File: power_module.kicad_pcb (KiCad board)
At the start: 2 copper layers, 6 parts, among them J1 USB_B, J2 CONN_01X02

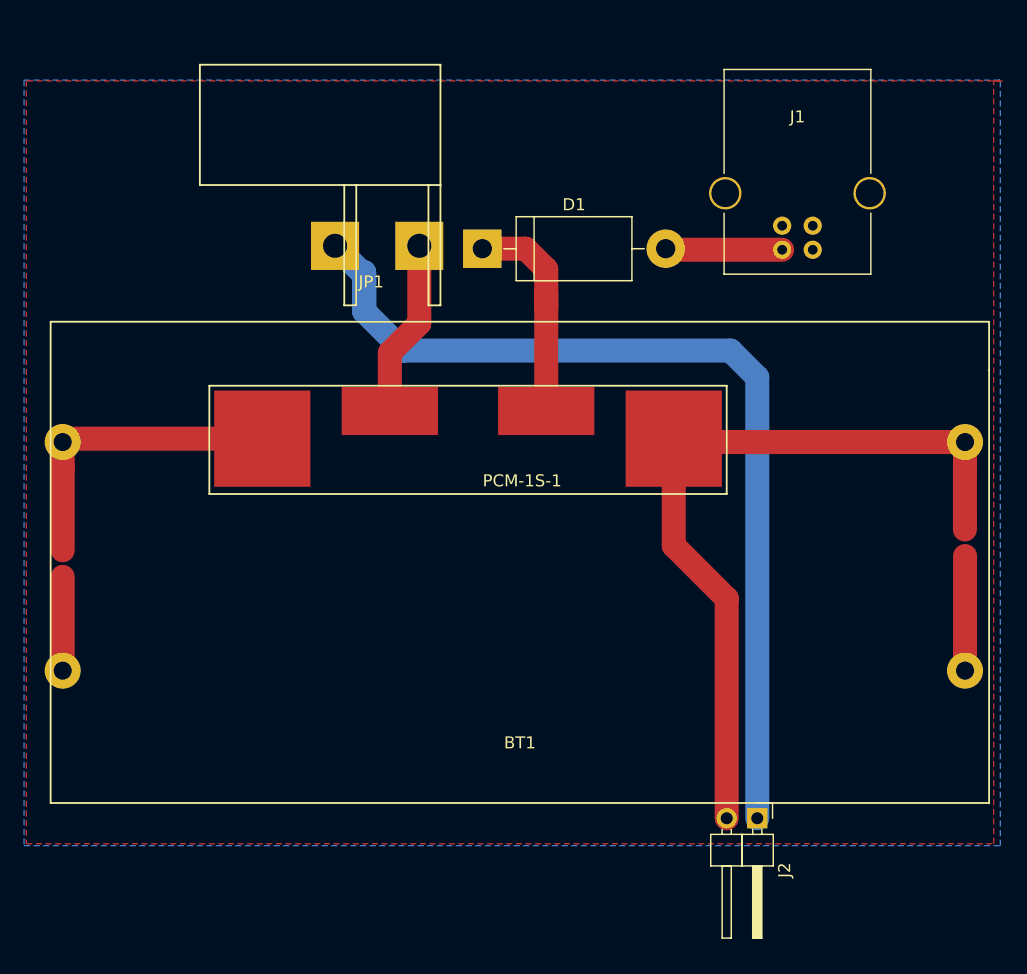
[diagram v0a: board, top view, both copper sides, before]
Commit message: add attiny 24-ssu
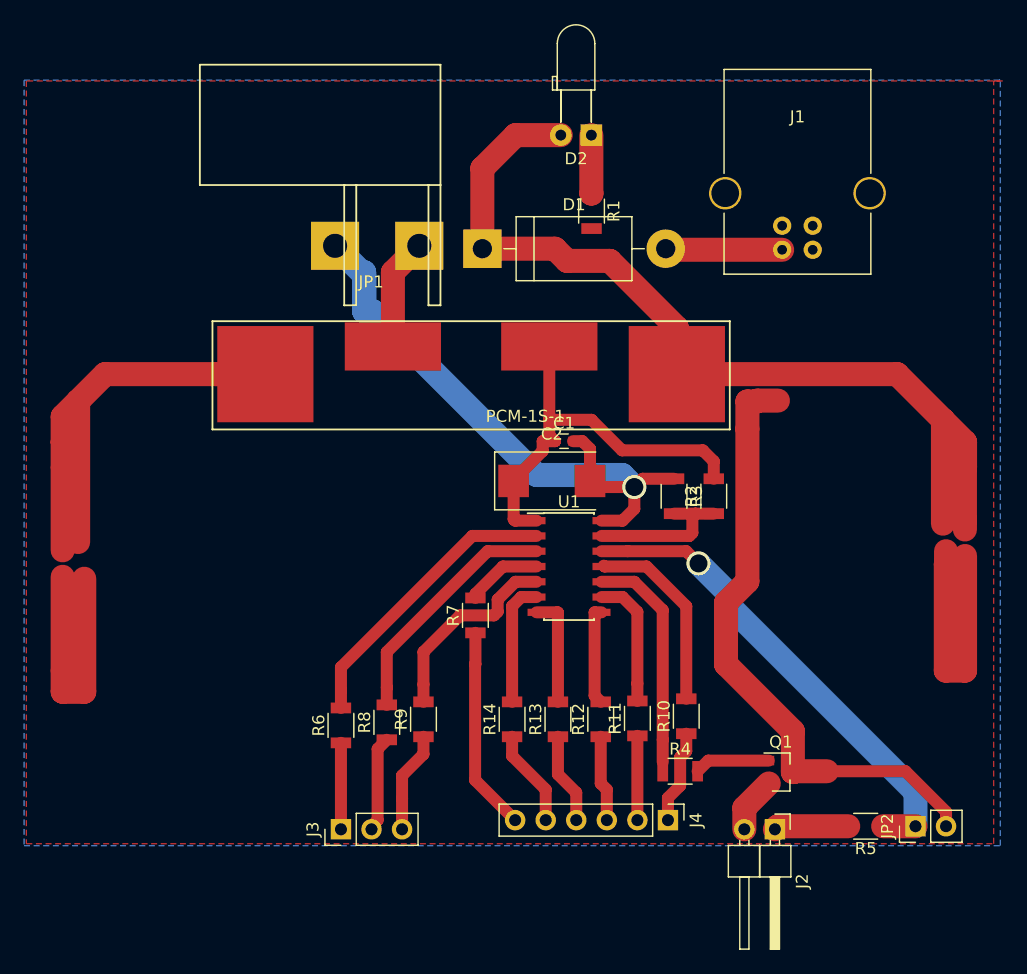
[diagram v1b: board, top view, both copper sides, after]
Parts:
- removed BT1: Battery, BH-18650-PC4
- added C1: 0.1uF, Capacitors_SMD:C_0603, F.Cu at (113.0, 67.3)
- added C2: 4.7uF, Capacitors_Tantalum_SMD:CP_Tantalum_Case-D_EIA-7343-31_Reflow, F.Cu at (112.0, 70.6)
- added D2: LED, LEDs:LED_D3.0mm_Horizontal_O3.81mm_Z6.0mm, F.Cu at (115.3, 41.9)
- added J3: CONN_01X03, Pin_Headers:Pin_Header_Straight_1x03_Pitch2.54mm, F.Cu at (94.5, 99.6)
- added J4: CONN_01X06, Pin_Headers:Pin_Header_Straight_1x06_Pitch2.54mm, F.Cu at (121.7, 98.8)
- added JP2: Jumper, Pin_Headers:Pin_Header_Straight_1x02_Pitch2.54mm, F.Cu at (142.2, 99.3)
- added Q1: Q_NMOS_GSD, TO_SOT_Packages_SMD:SOT-23, F.Cu at (131.0, 94.8)
- added R1: R, Resistors_SMD:R_1206, F.Cu at (115.3, 48.2)
- added R10: R, Resistors_SMD:R_1206, F.Cu at (123.2, 90.2)
- added R11: R, Resistors_SMD:R_1206, F.Cu at (119.1, 90.3)
- added R12: R, Resistors_SMD:R_1206, F.Cu at (116.1, 90.4)
- added R13: R, Resistors_SMD:R_1206, F.Cu at (112.5, 90.4)
- added R14: R, Resistors_SMD:R_1206, F.Cu at (108.7, 90.4)
- added R2: R, Resistors_SMD:R_1206, F.Cu at (125.5, 71.9)
- added R3: R, Resistors_SMD:R_1206, F.Cu at (122.2, 71.9)
- added R4: R, Resistors_SMD:R_1206, F.Cu at (122.7, 94.7)
- added R5: R, Resistors_SMD:R_1206, F.Cu at (138.1, 99.3)
- added R6: R, Resistors_SMD:R_1206, F.Cu at (94.5, 90.9)
- added R7: R, Resistors_SMD:R_1206, F.Cu at (105.7, 81.8)
- added R8: R, Resistors_SMD:R_1206, F.Cu at (98.3, 90.7)
- added R9: R, Resistors_SMD:R_1206, F.Cu at (101.3, 90.4)
- added U1: ATTINY24A-SSU, Housings_SOIC:SOIC-14_3.9x8.7mm_Pitch1.27mm, F.Cu at (113.4, 77.7)
- PCM-1S-1: footprint XZD-YH10A-1 -> XZD-YH10A-1:XZD-YH10A-1
- moved PCM-1S-1 5.37 mm to (105.8, 61.3)
- moved J2 1.73 mm to (130.6, 99.6)
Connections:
- J2 pad 2: Net-(BT1-Pad1) -> Net-(J2-Pad2)
- PCM-1S-1 pad 1: Net-(BT1-Pad1) -> +4V
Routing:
- net +4V: track 0.00 -> 87.1 mm
- net Net-(JP2-Pad1): track 0.00 -> 40.5 mm, vias 0 -> 1
- net (no net): track 17.3 -> 41.8 mm
- net Net-(R6-Pad2): track 0.00 -> 24.2 mm
- net Net-(R8-Pad2): track 0.00 -> 20.3 mm
- net Net-(C1-Pad2): track 81.3 -> 61.2 mm, vias 0 -> 1
- net Net-(R4-Pad1): track 0.00 -> 18.7 mm
- net Net-(J4-Pad6): track 0.00 -> 17.0 mm
- net Net-(R9-Pad2): track 0.00 -> 16.5 mm
- net Net-(R10-Pad2): track 0.00 -> 15.9 mm
- net Net-(BT1-Pad2): track 25.7 -> 41.5 mm
- net Net-(R2-Pad1): track 0.00 -> 12.7 mm
- net Net-(R11-Pad2): track 0.00 -> 10.9 mm
- net Net-(R14-Pad2): track 0.00 -> 10.3 mm
- net Net-(R13-Pad2): track 0.00 -> 9.20 mm
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
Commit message: Correct pcb
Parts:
- added BT1: Battery, BH-18650-PC4:BH-18650-PC4, F.Cu at (236.5, 65.5)
- added R15: 47K, Resistors_SMD:R_1206, F.Cu at (253.2, 80.5)
- C1: footprint Capacitors_SMD:C_0603 -> Capacitors_SMD:C_0805
- J2: value CONN_01X02 -> VOUT
- R1, R3: value R -> 330
- R2: value R -> 1.5K
- R4: value R -> 0
- R5: value R -> 47K
- moved J2 128.8 mm to (258.8, 87.9)
- moved C1 128.7 mm to (241.6, 59.7)
- moved R4 126.8 mm to (248.9, 83.3), turned to 180 degrees
- moved J1 126.7 mm to (257.4, 40.5)
- moved D1 126.7 mm to (232.5, 40.4)
- moved PCM-1S-1 126.7 mm to (232.0, 50.4)
- moved J3 126.7 mm to (220.7, 88.6)
- moved J4 126.7 mm to (247.9, 87.9)
- moved JP1 126.7 mm to (223.2, 40.1)
- moved Q1 126.7 mm to (257.3, 83.9)
- moved R10 126.7 mm to (249.4, 79.2)
- moved R11 126.7 mm to (245.4, 79.4)
- moved R12 126.7 mm to (242.3, 79.5)
- moved R2 126.7 mm to (251.7, 61.0)
- moved R3 126.7 mm to (248.4, 61.0)
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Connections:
- net Net-(C1-Pad2) renamed GNDA
- net Net-(J4-Pad6) renamed /reset
- net Net-(R11-Pad2) renamed /sck
- net Net-(R12-Pad2) renamed /miso
- net Net-(R13-Pad2) renamed /mosi
- net Net-(R14-Pad2) renamed /ss
- D2 pad 2: Net-(BT1-Pad1) -> +5V
- R4 pad 1: Net-(R4-Pad1) -> Net-(Q1-Pad1)
- R4 pad 2: Net-(Q1-Pad1) -> Net-(R4-Pad2)
- U1 pad 10: Net-(R4-Pad1) -> Net-(R4-Pad2)
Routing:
- net Net-(BT1-Pad1): track 79.3 -> 50.1 mm
- net Net-(R4-Pad2): track 0.00 -> 18.7 mm
- net Net-(R4-Pad1): track 18.7 -> 0.00 mm
- net +5V: track 9.92 -> 28.5 mm
- net GNDA: track 61.2 -> 79.0 mm, vias 1 -> 2
- net Net-(BT1-Pad2): track 41.5 -> 26.8 mm
- net (no net): track 41.8 -> 35.5 mm
- net +4V: track 87.1 -> 91.5 mm
- net Net-(Q1-Pad1): track 6.28 -> 8.65 mm
- net Net-(D2-Pad1): track 4.87 -> 2.86 mm
- net Net-(JP2-Pad1): track 40.5 -> 42.4 mm
- net Net-(J2-Pad2): track 4.65 -> 2.96 mm
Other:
- net class Default: clearance 0.2 -> 0.4; trace_width 2 -> 1
- rule trace_clearance: 0.2 -> 0.4
- rule trace_min: 2 -> 0.3
- rule via_min_size: 0.6 -> 0.5

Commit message: make last changes
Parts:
- moved J1 195.2 mm to (84.4, 131.0)
- moved BT1 195.2 mm to (63.5, 156.1)
- moved C1 195.2 mm to (68.6, 150.2)
- moved C2 195.2 mm to (60.2, 150.2)
- moved D1 195.2 mm to (59.5, 130.9)
- moved D2 195.2 mm to (64.5, 121.5)
- moved J2 195.2 mm to (85.9, 178.4)
- moved J3 195.2 mm to (47.8, 179.2)
- moved J4 195.2 mm to (75.0, 178.4)
- moved JP1 195.2 mm to (50.3, 130.7)
- moved JP2 195.2 mm to (95.3, 178.4)
- moved PCM-1S-1 195.2 mm to (59.1, 140.9)
- moved Q1 195.2 mm to (84.3, 174.4)
- moved R1 195.2 mm to (64.5, 125.8)
- moved R10 195.2 mm to (76.5, 169.8)
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
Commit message: Make it one side
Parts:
- added J5: CONN_01X02, Resistors_SMD:R_2512, F.Cu at (253.0, 44.9)
- added J6: CONN_01X02, Resistors_SMD:R_2512, F.Cu at (245.0, 54.9)
- added R16: 0, Resistors_SMD:R_1206, F.Cu at (240.0, 66.0)
- added R17: 0, Resistors_SMD:R_2512, F.Cu at (249.0, 70.0)
- D1, J1, JP1: moved to B.Cu
- moved JP1 209.8 mm to (237.0, 35.0), turned to 180 degrees
- moved R15 195.6 mm to (244.0, 64.0), turned to 90 degrees
- moved R1 195.2 mm to (234.0, 29.0), turned to 0 degrees
- moved J3 194.2 mm to (216.5, 83.0)
- moved J2 193.8 mm to (254.5, 83.0)
- moved D1 193.1 mm to (228.2, 37.0), turned to 180 degrees
- moved Q1 193.0 mm to (251.0, 77.0), turned to 90 degrees
- moved PCM-1S-1 192.6 mm to (226.0, 44.9)
- moved R4 192.1 mm to (235.0, 66.0)
- moved C2 192.0 mm to (227.0, 55.0)
- moved R6 191.7 mm to (214.0, 75.0)
- moved R8 190.9 mm to (217.0, 75.0)
- moved R9 190.7 mm to (220.0, 75.0)
- moved R14 189.5 mm to (226.0, 75.0)
- moved J4 189.4 mm to (238.5, 83.0)
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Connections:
- R15 pad 1: Net-(Q1-Pad1) -> Net-(R15-Pad1)
- R4 pad 1: Net-(Q1-Pad1) -> Net-(R15-Pad1)
- R5 pad 1: Net-(JP2-Pad1) -> Net-(R16-Pad1)
- U1 pad 12: Net-(JP2-Pad1) -> Net-(R16-Pad1)
- U1 pad 4: Net-(R7-Pad2) -> Net-(R9-Pad2)
- U1 pad 5: Net-(R9-Pad2) -> Net-(R7-Pad2)
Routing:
- net (no net): track 35.5 -> 0.00 mm
- net GNDA: track 79.0 -> 112.6 mm, vias 2 -> 0
- net Net-(JP2-Pad1): track 42.4 -> 17.4 mm, vias 1 -> 0
- net Net-(R4-Pad2): track 18.7 -> 4.45 mm
- net Net-(R15-Pad1): track 0.00 -> 14.0 mm
- net Net-(R16-Pad1): track 0.00 -> 13.3 mm
- net Net-(BT1-Pad1): track 50.1 -> 38.6 mm
- net /reset: track 17.0 -> 7.73 mm
- net Net-(R6-Pad2): track 24.2 -> 17.7 mm
- net Net-(R8-Pad2): track 20.3 -> 15.0 mm
- net Net-(R7-Pad2): track 6.35 -> 11.0 mm
- net Net-(R9-Pad2): track 16.5 -> 12.3 mm
- net Net-(BT1-Pad2): track 26.8 -> 22.8 mm
- net +4V: track 91.5 -> 94.9 mm
- net Net-(Q1-Pad1): track 8.65 -> 5.33 mm
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- removed copper zone on B.Cu, net GNDA
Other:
- net class Default: trace_width 1 -> 0.6
- net class power added: clearance 1, trace_width 2, via_dia 2, via_drill 1.5

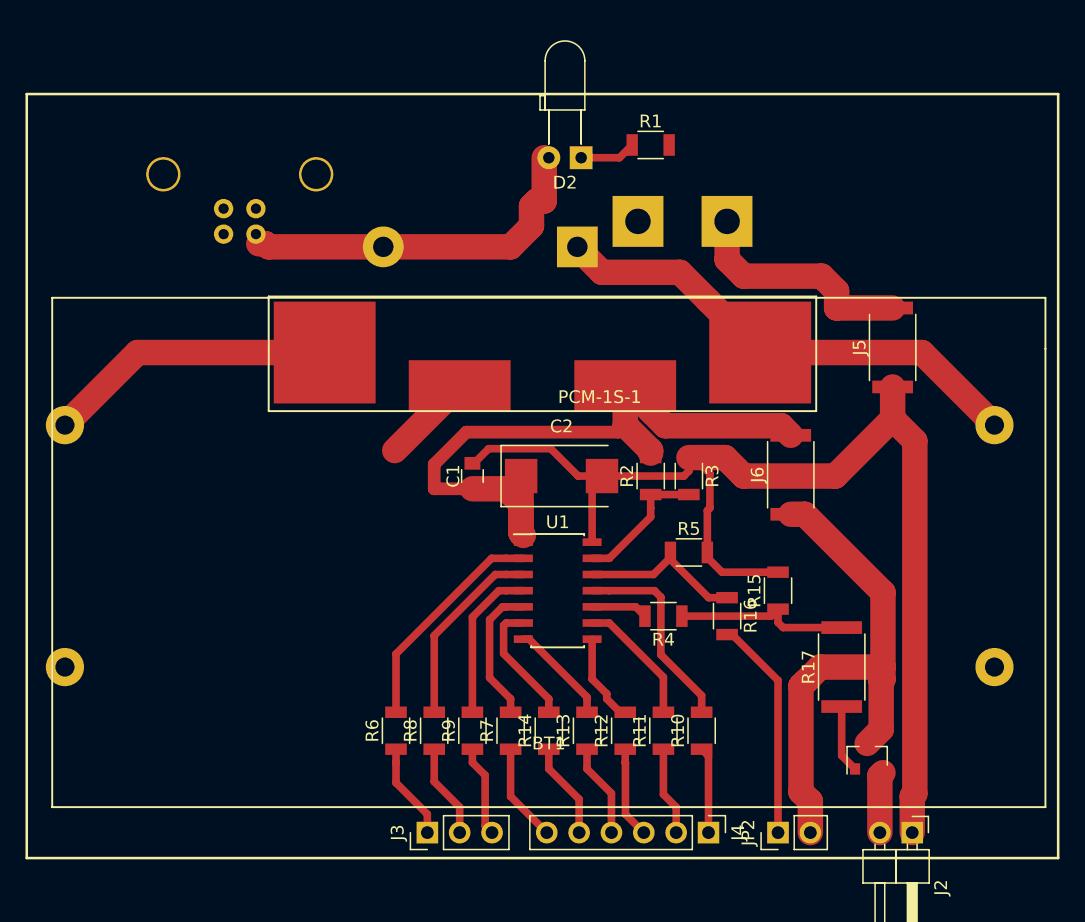
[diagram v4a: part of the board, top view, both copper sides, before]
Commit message: Поправил схему н-канального транзистора, обновил дорожки на плате, удалил не нужные файлы, поправил посадочные места для выключателя, поправил посадочное место для батареии 18650
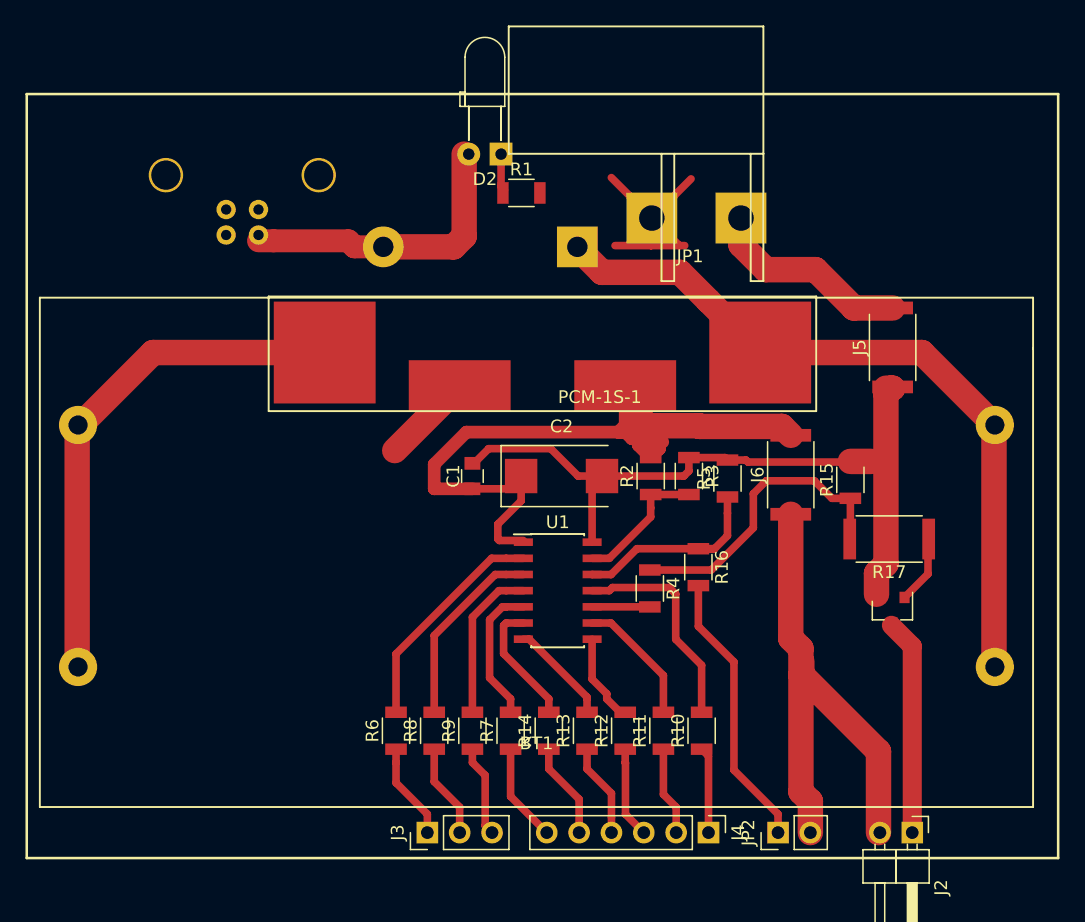
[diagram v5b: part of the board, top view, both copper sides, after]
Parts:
- BT1: footprint BH-18650-PC4:BH-18650-PC4 -> BH-18650-PC4
- JP1: moved to F.Cu
- moved Q1 11.6 mm to (253.0, 65.5), turned to 270 degrees
- moved R1 10.8 mm to (223.8, 32.8)
- moved R17 10.7 mm to (252.7, 59.9), turned to 180 degrees
- moved R15 10.4 mm to (249.7, 55.3)
- moved R5 6.55 mm to (240.0, 55.2), turned to 90 degrees
- moved D2 6.30 mm to (222.2, 29.7)
- moved R16 4.46 mm to (237.7, 62.2)
- moved R4 2.42 mm to (233.9, 63.8), turned to 270 degrees
- moved BT1 0.97 mm to (225.0, 61.0)
- moved JP1 0.28 mm to (237.1, 34.7), turned to 0 degrees
- moved J1 0.21 mm to (203.2, 36.1)
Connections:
- net Net-(J3-Pad2) renamed /led.red
- net Net-(R16-Pad1) renamed /pwr_btn
- J2 pad 1: GNDA -> Net-(J2-Pad1)
- J2 pad 2: Net-(J2-Pad2) -> +4V
- J3 pad 3: Net-(J3-Pad3) -> /reset
- J4 pad 6: /reset -> Net-(J4-Pad6)
- Q1 pad 2: Net-(J2-Pad2) -> GNDA
- Q1 pad 3: +4V -> Net-(J2-Pad1)
- R7 pad 1: /reset -> Net-(J4-Pad6)
- R9 pad 1: Net-(J3-Pad3) -> /reset
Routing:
- net GNDA: track 112.6 -> 75.0 mm
- net GND: track 7.21 -> 26.8 mm
- net Net-(BT1-Pad1): track 38.6 -> 57.6 mm
- net Net-(BT1-Pad2): track 22.8 -> 40.9 mm
- net Net-(J2-Pad1): track 0.00 -> 17.0 mm
- net +4V: track 94.9 -> 105.0 mm
- net Net-(R15-Pad1): track 14.0 -> 23.1 mm
- net Net-(J4-Pad6): track 0.00 -> 7.73 mm
- net Net-(J3-Pad3): track 7.19 -> 0.00 mm
- net +5V: track 28.3 -> 23.1 mm
- net Net-(J2-Pad2): track 4.88 -> 0.00 mm
- net Net-(JP2-Pad1): track 17.4 -> 22.0 mm
- net /pwr_btn: track 13.3 -> 16.2 mm
- net Net-(D2-Pad1): track 4.42 -> 2.90 mm
- net Net-(R10-Pad2): track 16.0 -> 17.0 mm
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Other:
- net class Default: clearance 0.4 -> 0
- net class power: clearance 1 -> 0.8
- rule trace_clearance: 0.4 -> 0

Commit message: Мелкие поправки по плате
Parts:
- BT1: footprint BH-18650-PC4 -> BH-18650-PC4:BH-18650-PC4
- moved R3 6.98 mm to (230.8, 58.3), turned to 0 degrees
- moved Q1 4.13 mm to (249.2, 67.3)
- moved R5 3.30 mm to (237.0, 56.5)
- moved J6 2.95 mm to (242.5, 56.5)
- moved R16 1.18 mm to (236.9, 61.4)
- moved R2 0.17 mm to (234.2, 54.9)
- moved BT1 0.11 mm to (225.0, 61.1)
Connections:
- net Net-(J3-Pad1) renamed /led.green
- R14 pad 2: /ss -> Net-(R14-Pad2)
- R7 pad 2: Net-(R7-Pad2) -> /ss
- U1 pad 5: Net-(R7-Pad2) -> /ss
- U1 pad 6: /ss -> Net-(R14-Pad2)
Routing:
- net Net-(R7-Pad2): track 11.0 -> 0.00 mm
- net Net-(R14-Pad2): track 0.00 -> 9.91 mm
- net /pwr_btn: track 16.2 -> 10.7 mm
- net Net-(Q1-Pad1): track 5.61 -> 9.97 mm
- net GNDA: track 75.0 -> 77.7 mm
- net +4V: track 105.0 -> 107.6 mm
- net Net-(R15-Pad1): track 23.1 -> 21.0 mm
- net Net-(J2-Pad1): track 17.0 -> 18.5 mm
- net /ss: track 9.91 -> 11.0 mm
- net Net-(JP2-Pad1): track 22.0 -> 23.1 mm
- net Net-(BT1-Pad1): track 57.6 -> 58.6 mm
- net Net-(R2-Pad1): track 10.7 -> 9.83 mm
